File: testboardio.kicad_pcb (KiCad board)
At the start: 2 copper layers, 120 x 59 mm, 35 parts, among them Q1 Q_NMOS_GSD, SW1 Rotary_Encoder_Switch, U1 Elite-C

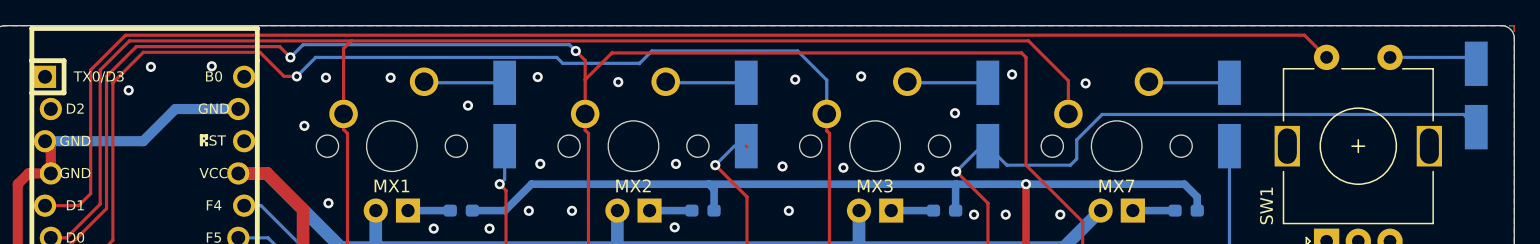
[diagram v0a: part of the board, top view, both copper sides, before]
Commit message: Moved D10
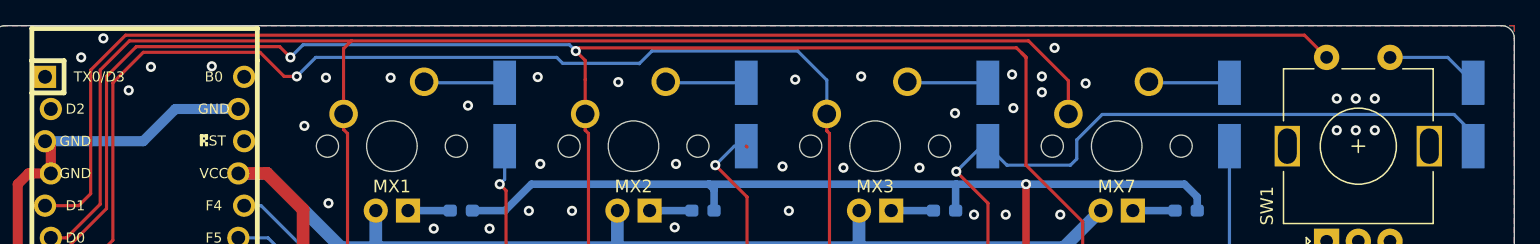
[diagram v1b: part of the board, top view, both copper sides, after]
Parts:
- moved D10 1.52 mm to (275.8, 61.0)
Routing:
- net R0: track 136.8 -> 137.8 mm
- net C1: track 142.4 -> 143.0 mm
- net Net-(D10-Pad2): track 7.01 -> 7.63 mm
- net GND: vias 75 -> 87
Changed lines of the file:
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@@
     (thickness 1.6)
     (drawings 8)
-    (tracks 375)
+    (tracks 390)
     (zones 0)
     (modules 35)
@@
   )
   (module Diode_SMD:D_SMA_Handsoldering (layer B.Cu)
-    (at 276 59.5 90)
+    (at 275.75 61 90)
     (descr "Diode SMA (DO-214AC) Handsoldering")
     (tags "Diode SMA (DO-214AC) Handsoldering")
     (attr smd)
-    (fp_text reference D10 (at 0 2.5 90) (layer B.SilkS)
+    (fp_text reference D10 (at 0 2.25 90) (layer B.SilkS)
       (effects (font (size 1 1) (thickness 0.15)) (justify mirror))
     )
@@
   (segment (start 216 65) (end 218.5 67.5) (width 0.25) (layer F.Cu) (net 2))
   (segment (start 244 65) (end 238.99 65) (width 0.25) (layer B.Cu) (net 2))
-  (segment (start 275 61) (end 246.5 61) (width 0.25) (layer B.Cu) (net 2))
   (segment (start 246.5 61) (end 244.5 63) (width 0.25) (layer B.Cu) (net 2))
-  (segment (start 276 62) (end 275 61) (width 0.25) (layer B.Cu) (net 2))
   (segment (start 238.99 65) (end 237.49 63.5) (width 0.25) (layer B.Cu) (net 2))
   (segment (start 244.5 64.5) (end 244 65) (width 0.25) (layer B.Cu) (net 2))
   (segment (start 244.5 63) (end 244.5 64.5) (width 0.25) (layer B.Cu) (net 2))
+  (segment (start 276 63.5) (end 276 62.75) (width 0.25) (layer B.Cu) (net 2))
+  (segment (start 276 62.75) (end 274.25 61) (width 0.25) (layer B.Cu) (net 2))
+  (segment (start 274.25 61) (end 246.5 61) (width 0.25) (layer B.Cu) (net 2))
   (segment (start 212.17 58.5) (end 212.09 58.42) (width 0.25) (layer B.Cu) (net 3))
   (segment (start 218.44 58.5) (end 212.17 58.5) (width 0.25) (layer B.Cu) (net 3))
@@
   (segment (start 244.964999 78.885001) (end 244.964999 69.464999) (width 0.25) (layer F.Cu) (net 17))
   (segment (start 240.5 56.5) (end 240.15002 56.15002) (width 0.25) (layer F.Cu) (net 17))
-  (segment (start 207.84998 56.15002) (end 205.74 58.26) (width 0.25) (layer F.Cu) (net 17))
   (segment (start 240.5 65) (end 240.5 56.5) (width 0.25) (layer F.Cu) (net 17))
   (segment (start 243.84 80.01) (end 244.964999 78.885001) (width 0.25) (layer F.Cu) (net 17))
-  (segment (start 240.15002 56.15002) (end 207.84998 56.15002) (width 0.25) (layer F.Cu) (net 17))
+  (segment (start 205.25 55.75) (end 205 56) (width 0.25) (layer F.Cu) (net 17))
+  (segment (start 240.5 56.5) (end 239.75 55.75) (width 0.25) (layer F.Cu) (net 17))
+  (segment (start 239.75 55.75) (end 205.25 55.75) (width 0.25) (layer F.Cu) (net 17))
   (segment (start 229.87 68.58) (end 233.2 68.58) (width 0.6) (layer B.Cu) (net 18))
   (segment (start 224.79 60.96) (end 224.79 62.29) (width 0.25) (layer F.Cu) (net 19))
@@
   (via (at 233 98.75) (size 0.8) (drill 0.4) (layers F.Cu B.Cu) (net 27))
   (via (at 233 100) (size 0.8) (drill 0.4) (layers F.Cu B.Cu) (net 27))
+  (via (at 167.75 55) (size 0.8) (drill 0.4) (layers F.Cu B.Cu) (net 27))
+  (via (at 166 56.5) (size 0.8) (drill 0.4) (layers F.Cu B.Cu) (net 27))
+  (via (at 241.75 59.25) (size 0.8) (drill 0.4) (layers F.Cu B.Cu) (net 27))
+  (via (at 241.75 58) (size 0.8) (drill 0.4) (layers F.Cu B.Cu) (net 27))
+  (via (at 239.5 60.5) (size 0.8) (drill 0.4) (layers F.Cu B.Cu) (net 27))
+  (via (at 242.75 55.75) (size 0.8) (drill 0.4) (layers F.Cu B.Cu) (net 27))
+  (via (at 265 59.75) (size 0.8) (drill 0.4) (layers F.Cu B.Cu) (net 27))
+  (via (at 266.5 59.75) (size 0.8) (drill 0.4) (layers F.Cu B.Cu) (net 27))
+  (via (at 268 59.75) (size 0.8) (drill 0.4) (layers F.Cu B.Cu) (net 27))
+  (via (at 265 62.25) (size 0.8) (drill 0.4) (layers F.Cu B.Cu) (net 27))
+  (via (at 268 62.25) (size 0.8) (drill 0.4) (layers F.Cu B.Cu) (net 27))
+  (via (at 266.5 62.25) (size 0.8) (drill 0.4) (layers F.Cu B.Cu) (net 27))
   (segment (start 244.875 100.575) (end 244.95 100.5) (width 0.25) (layer B.Cu) (net 28))
   (segment (start 244.875 103) (end 244.875 100.575) (width 0.25) (layer B.Cu) (net 28))
@@
   (segment (start 178.3914 90.8914) (end 178.3914 85.97) (width 0.25) (layer B.Cu) (net 29))
   (segment (start 244.875 105.125) (end 241 109) (width 0.25) (layer B.Cu) (net 29))
-  (segment (start 275.5 56.5) (end 276 57) (width 0.25) (layer B.Cu) (net 45))
-  (segment (start 269.2 56.5) (end 275.5 56.5) (width 0.25) (layer B.Cu) (net 45))
+  (segment (start 275.75 58.5) (end 273.75 56.5) (width 0.25) (layer B.Cu) (net 45))
+  (segment (start 276 58.5) (end 275.75 58.5) (width 0.25) (layer B.Cu) (net 45))
+  (segment (start 269.2 56.5) (end 273.75 56.5) (width 0.25) (layer B.Cu) (net 45))
   (segment (start 166.75 57.5) (end 169.5 54.75) (width 0.25) (layer F.Cu) (net 46))
   (segment (start 166.75 67.25) (end 166.75 57.5) (width 0.25) (layer F.Cu) (net 46))
